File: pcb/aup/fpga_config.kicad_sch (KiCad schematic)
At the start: 1 part, among them U1 XC7A50T-2FGG484C

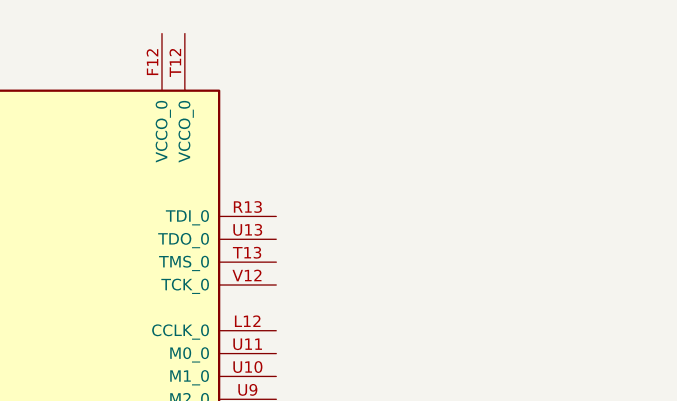
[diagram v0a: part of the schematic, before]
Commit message: Added more passives
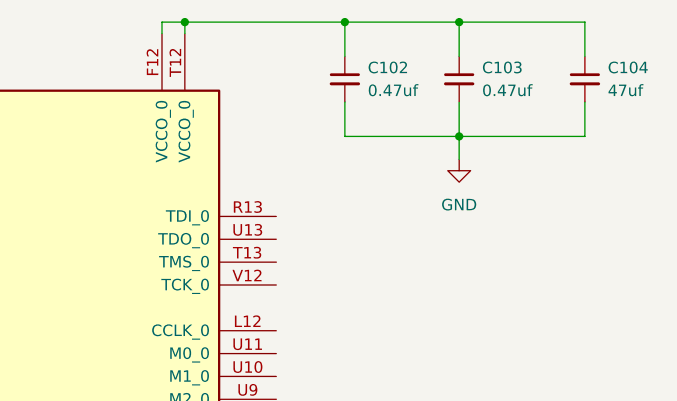
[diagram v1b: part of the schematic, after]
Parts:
- added C102, C103: 0.47uf, Capacitor_SMD:C_0402_1005Metric, symbol !Misc:C_0.47uf_0402
- added C104: 47uf, Capacitor_SMD:C_1206_3216Metric, symbol !Misc:C_47uf_1206
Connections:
- net GND: now also C102.2, C103.2, C104.2
- net at U1.F12 (VCCO_0): now also U1.T12 (VCCO_0), C102.1, C103.1, C104.1

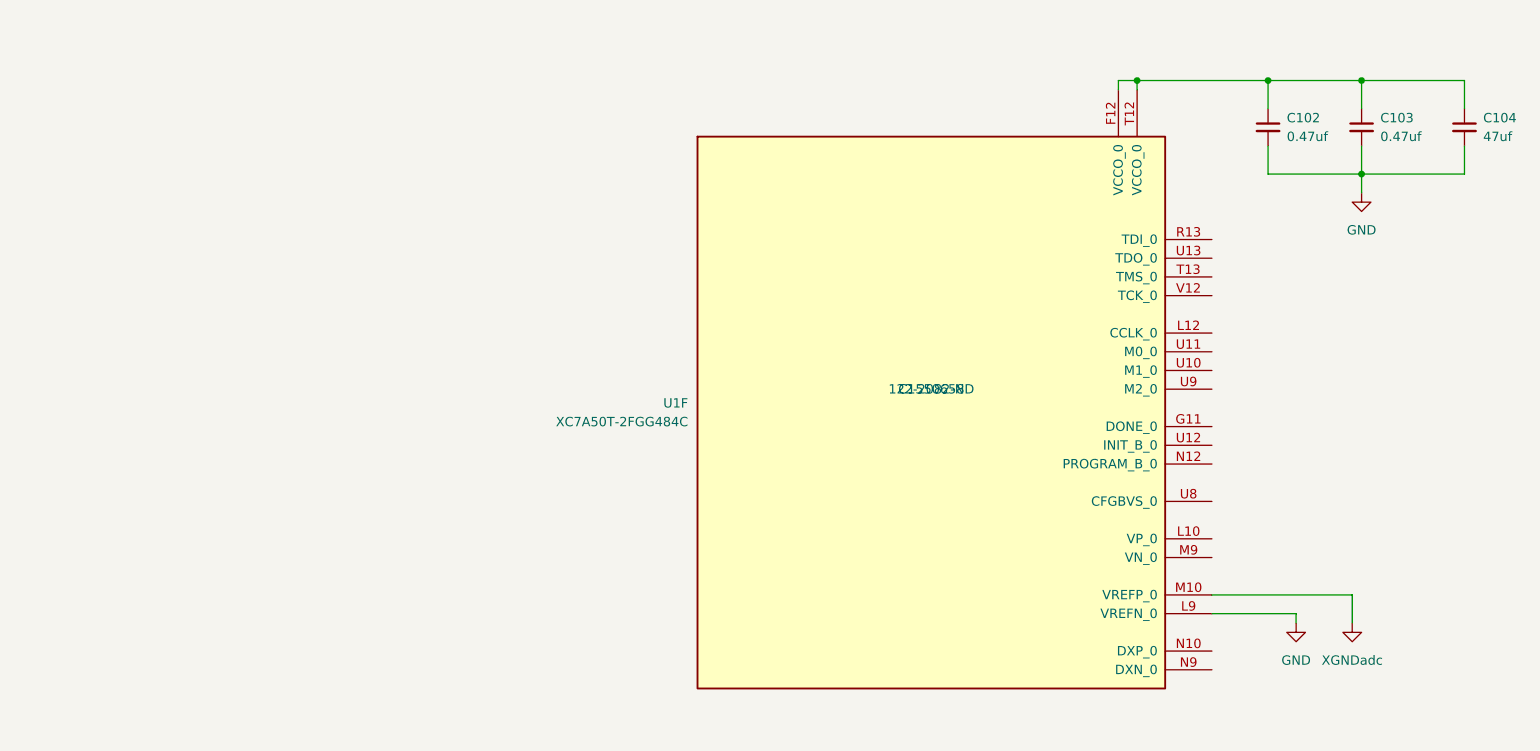
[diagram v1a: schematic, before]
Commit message: Switch 0.47uf caps under bga to 0201
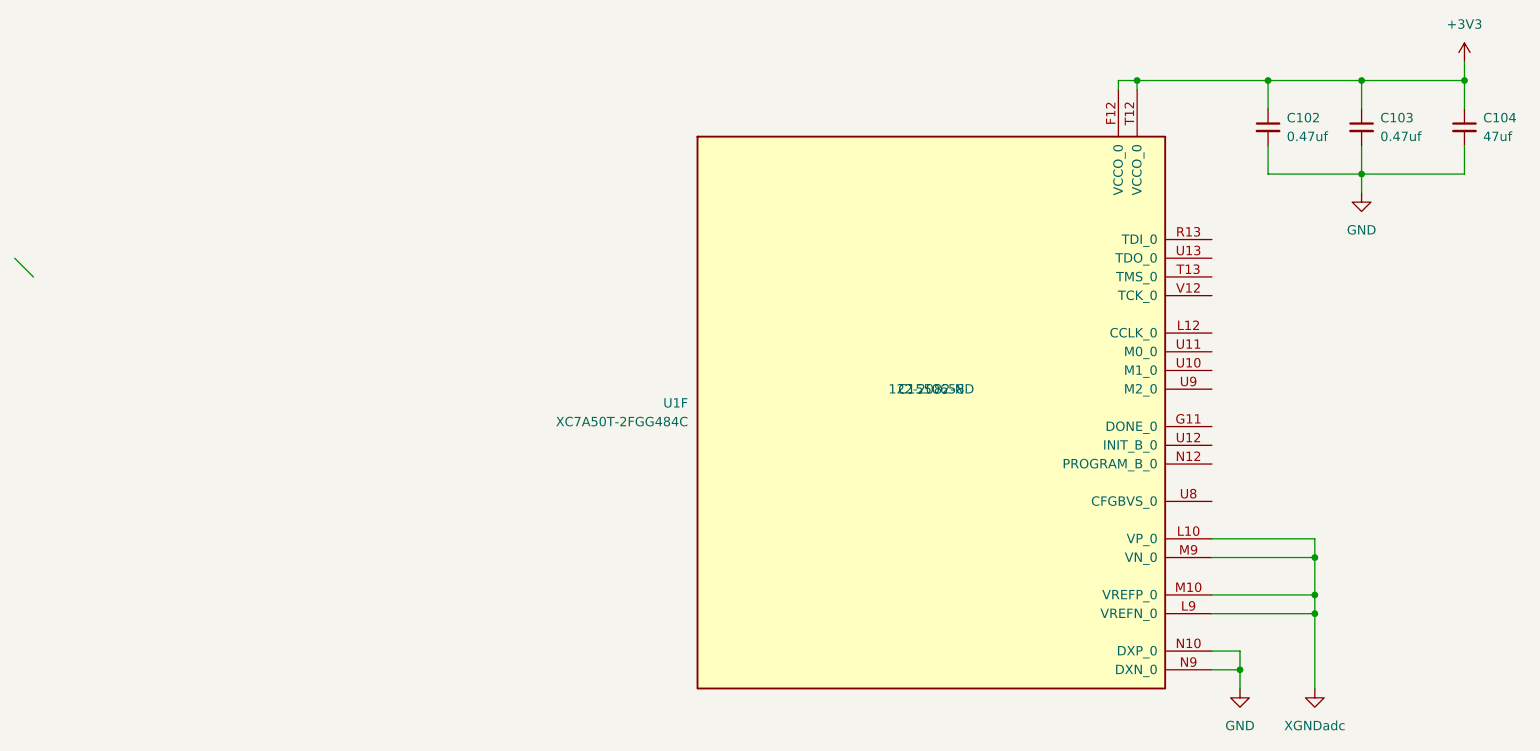
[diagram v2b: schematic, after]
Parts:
- C102, C103: footprint Capacitor_SMD:C_0402_1005Metric -> Capacitor_SMD:C_0201_0603Metric; symbol !Misc:C_0.47uf_0402 -> !Misc:C_0.47uf_0201; Digi-Key Part Number 1276-1173-1-ND -> 1276-1337-1-ND; LCSC Part # C1779 -> C318543
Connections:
- net GND: now also U1.N10 (DXP_0), U1.N9 (DXN_0); no longer U1.L9 (VREFN_0)
- net XGNDadc: now also U1.L10 (VP_0), U1.L9 (VREFN_0), U1.M9 (VN_0)
- net +3V3: now reaches C102.1, C103.1, C104.1, U1.F12 (VCCO_0), U1.T12 (VCCO_0)
